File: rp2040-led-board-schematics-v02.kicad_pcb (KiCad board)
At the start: 4 copper layers, 161 x 99 mm, 127 parts, among them J1 PWR_IN, J12 ReceiverRS485, J13 MainBoard, J14 Terminal, J15 Terminal, J16 Terminal, J17 Terminal, J18 Terminal, J19 Terminal, J2 Terminal, J20 Terminal, J5 FrontPanel, J8 ReceiverData, SW1 Button, SW2 PEC16, U1 LM7805, U10 MAX485E, U11 MAX485E, U12 ENC28J60, U13 LM7805, U2 MAX485E, U3 MAX485E, U4 MAX485E, U5 MAX485E, U6 MAX485E, U7 Pico, U8 MAX485E, U9 MAX485E

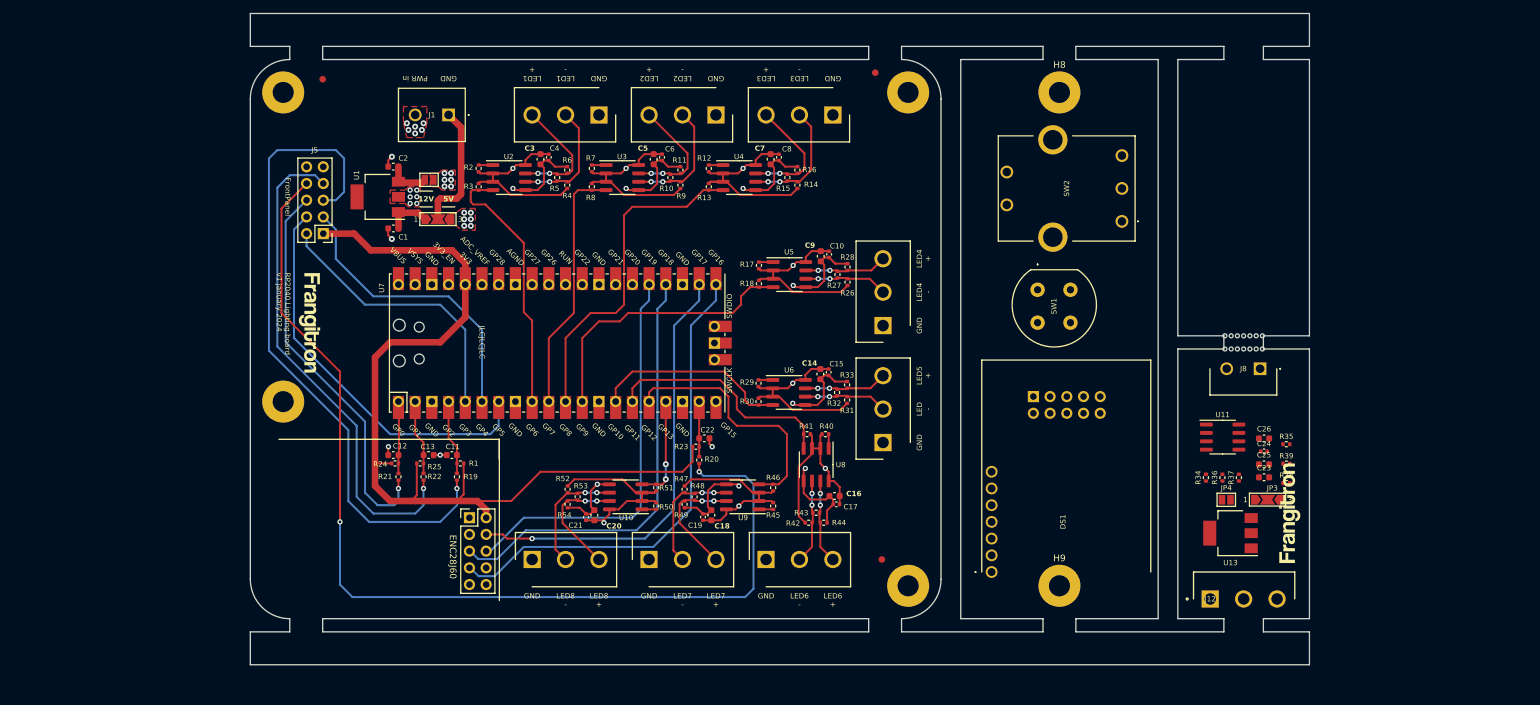
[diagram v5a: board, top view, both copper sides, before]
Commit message: receiver layout OK, some references fixed
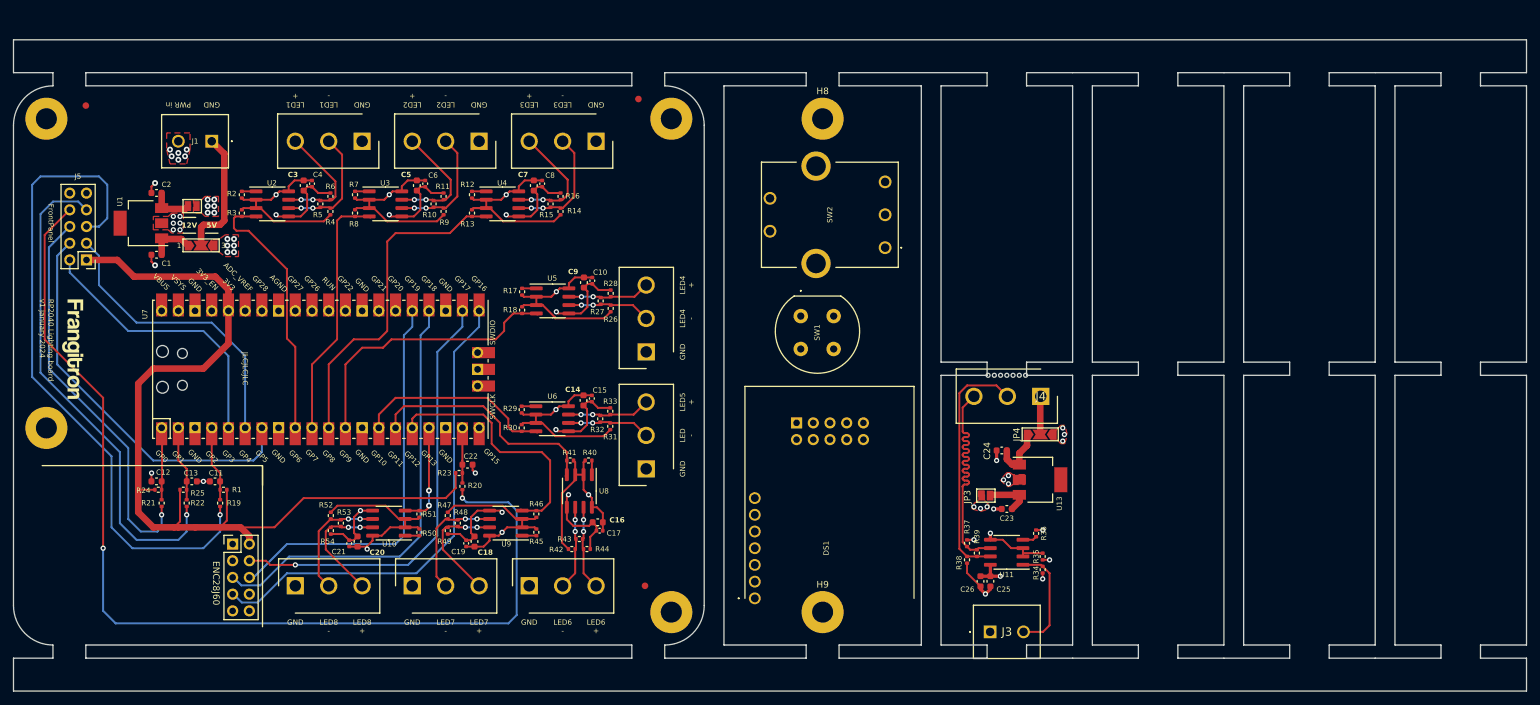
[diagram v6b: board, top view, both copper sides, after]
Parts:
- removed H10: ~, Library:mouse-bites-1x07-jlc
- removed J12: ReceiverRS485, Frangitron:ScrewTerminal_01x03_5.08_Amphenol
- removed J8: ReceiverData, Frangitron:ScrewTerminal_01x02_5.08_Amphenol
- added J3: ReceiverData, Frangitron:ScrewTerminal_01x02_5.08_Amphenol, F.Cu at (186.5, 138.0)
- added J4: ReceiverRS485, Frangitron:ScrewTerminal_01x03_5.08_Amphenol, F.Cu at (194.2, 102.2)
- C24: value 10uF -> 220nF; footprint Capacitor_SMD:C_0402_1005Metric -> Capacitor_SMD:C_0603_1608Metric
- C25: value 220nF -> 100nF
- C26: value 100nF -> 10uF
- H6: moved to B.Cu
- JP3: footprint Jumper:SolderJumper-3_P2.0mm_Open_TrianglePad1.0x1.5mm_NumberLabels -> Jumper:SolderJumper-2_P1.3mm_Open_Pad1.0x1.5mm
- JP4: footprint Jumper:SolderJumper-2_P1.3mm_Open_Pad1.0x1.5mm -> Jumper:SolderJumper-3_P2.0mm_Open_TrianglePad1.0x1.5mm_NumberLabels
- R35: value 20K -> 10K
- R37: value 10K -> 20K
- R38: value 120 -> 20K
- R39: value 20K -> 120
- moved H6 63.0 mm to (173.0, 98.0), turned to -90 degrees
- moved R38 49.9 mm to (182.9, 127.1), turned to -90 degrees
- moved R39 49.0 mm to (184.4, 126.0), turned to 90 degrees
- moved C26 48.3 mm to (185.0, 130.3), turned to -90 degrees
- moved C25 45.2 mm to (186.5, 130.3), turned to -90 degrees
- moved JP3 42.8 mm to (185.8, 117.3)
- moved R37 42.5 mm to (182.9, 124.5), turned to -90 degrees
- moved R35 40.8 mm to (194.4, 126.6), turned to 90 degrees
- moved C24 39.9 mm to (188.2, 110.4), turned to 180 degrees
- moved C23 39.4 mm to (189.0, 119.3), turned to 180 degrees
- moved U11 37.2 mm to (189.0, 125.9), turned to 180 degrees
- moved C5 36.2 mm to (99.3, 70.2)
- moved C7 36.2 mm to (117.1, 70.2)
- moved C9 36.2 mm to (124.7, 84.9)
- moved R12 36.2 mm to (107.7, 71.5)
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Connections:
- net /LED to RS485/D+ renamed /LED to RS485 1/D+
- net /LED to RS485/D- renamed /LED to RS485 1/D-
- net /LED to RS486/D+ renamed /LED to RS485 2/D+
- net /LED to RS486/D- renamed /LED to RS485 2/D-
- net /LED to RS487/D+ renamed /LED to RS485 3/D+
- net /LED to RS487/D- renamed /LED to RS485 3/D-
- net /LED to RS488/D+ renamed /LED to RS485 4/D+
- net /LED to RS488/D- renamed /LED to RS485 4/D-
- net /LED to RS489/D+ renamed /LED to RS485 5/D+
- net /LED to RS489/D- renamed /LED to RS485 5/D-
- net /LED to RS490/D+ renamed /LED to RS485 6/D+
- net /LED to RS490/D- renamed /LED to RS485 6/D-
- net /LED to RS491/D+ renamed /LED to RS485 7/D+
- net /LED to RS491/D- renamed /LED to RS485 7/D-
- net /LED to RS492/D+ renamed /LED to RS485 8/D+
- net /LED to RS492/D- renamed /LED to RS485 8/D-
- net Net-(J12-Pin_2) renamed /Receiver1/D+
- net Net-(J8-Pin_2) renamed /Receiver1/DATA
- C23 pad 2: Recv GND -> /Receiver1/GND
- C24 pad 1: Recv +5V -> /Receiver1/12V
- C24 pad 2: Recv GND -> /Receiver1/GND
- C25 pad 1: Net-(JP4-A) -> /Receiver1/5V
- C25 pad 2: Recv GND -> /Receiver1/GND
- C26 pad 1: Recv +5V -> /Receiver1/5V
- C26 pad 2: Recv GND -> /Receiver1/GND
- JP3 pad 1: Recv +5V -> /Receiver1/5V
- JP4 pad 1: Net-(JP4-A) -> /Receiver1/12V
- JP4 pad 2: Recv PWR -> /Receiver1/PWR IN
- R34 pad 1: Recv +5V -> /Receiver1/5V
- R35 pad 1: Recv +5V -> /Receiver1/5V
- R35 pad 2: Net-(J12-Pin_3) -> /Receiver1/GND
- R36 pad 1: Recv +5V -> /Receiver1/5V
- R36 pad 2: Recv GND -> Net-(U11-DI)
- R37 pad 1: Recv +5V -> /Receiver1/5V
- R37 pad 2: Net-(U11-DI) -> /Receiver1/D-
- R38 pad 2: Net-(J12-Pin_3) -> /Receiver1/GND
- R39 pad 2: Recv GND -> /Receiver1/D-
- U11 pad 2: Recv GND -> /Receiver1/GND
- U11 pad 3: Recv GND -> /Receiver1/GND
- U11 pad 5: Recv GND -> /Receiver1/GND
- U11 pad 6: Net-(J12-Pin_3) -> /Receiver1/D-
- U11 pad 8: Recv +5V -> /Receiver1/5V
- U13 pad 1: Net-(JP4-A) -> /Receiver1/12V
- U13 pad 2: Recv GND -> /Receiver1/GND
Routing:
- net /Receiver1/D+: track 0.00 -> 37.3 mm
- net /Receiver1/D-: track 0.00 -> 37.3 mm
- net /Receiver1/GND: track 0.00 -> 20.9 mm, vias 0 -> 7
- net /Receiver1/DATA: track 0.00 -> 16.9 mm
- net /Receiver1/5V: track 0.00 -> 9.01 mm, vias 0 -> 11
- net /Receiver1/12V: track 0.00 -> 8.63 mm
- net Net-(JP3-B): track 0.00 -> 7.10 mm
- net /Receiver1/PWR IN: track 0.00 -> 5.83 mm
- net Net-(U11-DI): track 0.00 -> 2.19 mm
- added copper zone on F.Cu, net /Receiver1/5V
- added copper zone on In2.Cu, net /Receiver1/5V
- added copper zone on F.Cu, net /Receiver1/GND
- added copper zone on In1.Cu, net /Receiver1/GND
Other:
- board size 161 x 99 mm -> 230 x 99 mm

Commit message: OK for first fabrication review
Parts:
- added C27: 100nF, Capacitor_SMD:C_0603_1608Metric, F.Cu at (190.3, 76.7)
- added C28: 100nF, Capacitor_SMD:C_0603_1608Metric, F.Cu at (191.5, 65.7)
- added C29: 220nF, Capacitor_SMD:C_0603_1608Metric, F.Cu at (191.6, 85.6)
- added C30: 10uF, Capacitor_SMD:C_0402_1005Metric, F.Cu at (193.0, 65.7)
- added C31: 100nF, Capacitor_SMD:C_0603_1608Metric, F.Cu at (210.7, 119.3)
- added C32: 100nF, Capacitor_SMD:C_0603_1608Metric, F.Cu at (209.5, 130.3)
- added C33: 220nF, Capacitor_SMD:C_0603_1608Metric, F.Cu at (209.4, 110.4)
- added C34: 10uF, Capacitor_SMD:C_0402_1005Metric, F.Cu at (208.0, 130.3)
- added C35: 100nF, Capacitor_SMD:C_0603_1608Metric, F.Cu at (213.3, 76.7)
- added C36: 100nF, Capacitor_SMD:C_0603_1608Metric, F.Cu at (214.5, 65.7)
- added C37: 220nF, Capacitor_SMD:C_0603_1608Metric, F.Cu at (214.6, 85.6)
- added C38: 10uF, Capacitor_SMD:C_0402_1005Metric, F.Cu at (216.0, 65.7)
- added C39: 100nF, Capacitor_SMD:C_0603_1608Metric, F.Cu at (233.7, 119.3)
- added C40: 100nF, Capacitor_SMD:C_0603_1608Metric, F.Cu at (232.5, 130.3)
- added C41: 220nF, Capacitor_SMD:C_0603_1608Metric, F.Cu at (232.4, 110.4)
- added C42: 10uF, Capacitor_SMD:C_0402_1005Metric, F.Cu at (231.0, 130.3)
- added C43: 100nF, Capacitor_SMD:C_0603_1608Metric, F.Cu at (236.3, 76.7)
- added C44: 100nF, Capacitor_SMD:C_0603_1608Metric, F.Cu at (237.5, 65.7)
- added C45: 220nF, Capacitor_SMD:C_0603_1608Metric, F.Cu at (237.6, 85.6)
- added C46: 10uF, Capacitor_SMD:C_0402_1005Metric, F.Cu at (239.0, 65.7)
- added C47: 100nF, Capacitor_SMD:C_0603_1608Metric, F.Cu at (256.7, 119.3)
- added C48: 100nF, Capacitor_SMD:C_0603_1608Metric, F.Cu at (255.5, 130.3)
- added C49: 220nF, Capacitor_SMD:C_0603_1608Metric, F.Cu at (255.4, 110.4)
- added C50: 10uF, Capacitor_SMD:C_0402_1005Metric, F.Cu at (254.0, 130.3)
- added C51: 100nF, Capacitor_SMD:C_0603_1608Metric, F.Cu at (259.3, 76.7)
- added C52: 100nF, Capacitor_SMD:C_0603_1608Metric, F.Cu at (260.5, 65.7)
- added C53: 220nF, Capacitor_SMD:C_0603_1608Metric, F.Cu at (260.6, 85.6)
- added C54: 10uF, Capacitor_SMD:C_0402_1005Metric, F.Cu at (262.0, 65.7)
- added FM4: Fiducial, Fiducial:Fiducial_1mm_Mask2mm, F.Cu at (44.5, 145.5)
- added H10: ~, Frangitron:frangitron_logo_16mm, B.Cu at (189.0, 62.0)
- added H12: ~, Library:mouse-bites-1x07-jlc, F.Cu at (189.0, 97.0)
- added H13: ~, Frangitron:frangitron_logo_16mm, B.Cu at (212.0, 134.0)
- added H14: ~, Library:mouse-bites-1x07-jlc, F.Cu at (212.0, 99.0)
- added H15: ~, Frangitron:frangitron_logo_16mm, B.Cu at (212.0, 62.0)
- added H16: ~, Library:mouse-bites-1x07-jlc, F.Cu at (212.0, 97.0)
- added H17: ~, Frangitron:frangitron_logo_16mm, B.Cu at (235.0, 134.0)
- added H18: ~, Library:mouse-bites-1x07-jlc, F.Cu at (235.0, 99.0)
- added H19: ~, Frangitron:frangitron_logo_16mm, B.Cu at (235.0, 62.0)
- added H20: ~, Library:mouse-bites-1x07-jlc, F.Cu at (235.0, 97.0)
- added H21: ~, Frangitron:frangitron_logo_16mm, B.Cu at (258.0, 134.0)
- added H22: ~, Library:mouse-bites-1x07-jlc, F.Cu at (258.0, 99.0)
- added H23: ~, Frangitron:frangitron_logo_16mm, B.Cu at (258.0, 62.0)
- added H24: ~, Library:mouse-bites-1x07-jlc, F.Cu at (258.0, 97.0)
- added H25: MountingHole, MountingHole:MountingHole_2mm, F.Cu at (40.5, 50.5)
- added H26: MountingHole, MountingHole:MountingHole_2mm, F.Cu at (40.5, 144.5)
- added H27: MountingHole, MountingHole:MountingHole_2mm, F.Cu at (265.5, 144.5)
- added H28: MountingHole, MountingHole:MountingHole_2mm, F.Cu at (265.5, 50.5)
- added J10: ReceiverData, Frangitron:ScrewTerminal_01x02_5.08_Amphenol, F.Cu at (214.5, 58.0)
- added J11: ReceiverRS485, Frangitron:ScrewTerminal_01x03_5.08_Amphenol, F.Cu at (206.8, 93.8)
- added J12: ReceiverData, Frangitron:ScrewTerminal_01x02_5.08_Amphenol, F.Cu at (232.5, 138.0)
- added J21: ReceiverRS485, Frangitron:ScrewTerminal_01x03_5.08_Amphenol, F.Cu at (240.2, 102.2)
- added J22: ReceiverData, Frangitron:ScrewTerminal_01x02_5.08_Amphenol, F.Cu at (237.5, 58.0)
- added J23: ReceiverRS485, Frangitron:ScrewTerminal_01x03_5.08_Amphenol, F.Cu at (229.8, 93.8)
- added J24: ReceiverData, Frangitron:ScrewTerminal_01x02_5.08_Amphenol, F.Cu at (255.5, 138.0)
- added J25: ReceiverRS485, Frangitron:ScrewTerminal_01x03_5.08_Amphenol, F.Cu at (263.2, 102.2)
- added J26: ReceiverData, Frangitron:ScrewTerminal_01x02_5.08_Amphenol, F.Cu at (260.5, 58.0)
- added J27: ReceiverRS485, Frangitron:ScrewTerminal_01x03_5.08_Amphenol, F.Cu at (252.8, 93.8)
- added J6: ReceiverData, Frangitron:ScrewTerminal_01x02_5.08_Amphenol, F.Cu at (191.6, 58.0)
- added J7: ReceiverRS485, Frangitron:ScrewTerminal_01x03_5.08_Amphenol, F.Cu at (183.9, 93.8)
- added J8: ReceiverData, Frangitron:ScrewTerminal_01x02_5.08_Amphenol, F.Cu at (209.5, 138.0)
- added J9: ReceiverRS485, Frangitron:ScrewTerminal_01x03_5.08_Amphenol, F.Cu at (217.2, 102.2)
- added JP10: 1-2 12V, Jumper:SolderJumper-3_P2.0mm_Open_TrianglePad1.0x1.5mm_NumberLabels, F.Cu at (206.9, 88.0)
- added JP11: 12V, Jumper:SolderJumper-2_P1.3mm_Open_Pad1.0x1.5mm, F.Cu at (230.5, 117.3)
- added JP12: 1-2 12V, Jumper:SolderJumper-3_P2.0mm_Open_TrianglePad1.0x1.5mm_NumberLabels, F.Cu at (240.1, 108.0)
- added JP13: 12V, Jumper:SolderJumper-2_P1.3mm_Open_Pad1.0x1.5mm, F.Cu at (239.5, 78.7)
- added JP14: 1-2 12V, Jumper:SolderJumper-3_P2.0mm_Open_TrianglePad1.0x1.5mm_NumberLabels, F.Cu at (229.9, 88.0)
- added JP15: 12V, Jumper:SolderJumper-2_P1.3mm_Open_Pad1.0x1.5mm, F.Cu at (253.5, 117.3)
- added JP16: 1-2 12V, Jumper:SolderJumper-3_P2.0mm_Open_TrianglePad1.0x1.5mm_NumberLabels, F.Cu at (263.1, 108.0)
- added JP17: 12V, Jumper:SolderJumper-2_P1.3mm_Open_Pad1.0x1.5mm, F.Cu at (262.5, 78.7)
- added JP18: 1-2 12V, Jumper:SolderJumper-3_P2.0mm_Open_TrianglePad1.0x1.5mm_NumberLabels, F.Cu at (252.9, 88.0)
- added JP5: 12V, Jumper:SolderJumper-2_P1.3mm_Open_Pad1.0x1.5mm, F.Cu at (193.5, 78.7)
- added JP6: 1-2 12V, Jumper:SolderJumper-3_P2.0mm_Open_TrianglePad1.0x1.5mm_NumberLabels, F.Cu at (183.9, 88.0)
- added JP7: 12V, Jumper:SolderJumper-2_P1.3mm_Open_Pad1.0x1.5mm, F.Cu at (207.5, 117.3)
- added JP8: 1-2 12V, Jumper:SolderJumper-3_P2.0mm_Open_TrianglePad1.0x1.5mm_NumberLabels, F.Cu at (217.1, 108.0)
- added JP9: 12V, Jumper:SolderJumper-2_P1.3mm_Open_Pad1.0x1.5mm, F.Cu at (216.5, 78.7)
- added R55: 10K, Resistor_SMD:R_0402_1005Metric, F.Cu at (183.6, 67.4)
- added R56: 10K, Resistor_SMD:R_0402_1005Metric, F.Cu at (183.6, 69.4)
- added R57: 10K, Resistor_SMD:R_0402_1005Metric, F.Cu at (184.6, 73.0)
- added R58: 20K, Resistor_SMD:R_0402_1005Metric, F.Cu at (195.1, 71.1)
- added R59: 20K, Resistor_SMD:R_0402_1005Metric, F.Cu at (195.1, 68.9)
- added R60: 120, Resistor_SMD:R_0402_1005Metric, F.Cu at (193.6, 70.0)
- added R61: 10K, Resistor_SMD:R_0402_1005Metric, F.Cu at (217.4, 128.6)
- added R62: 10K, Resistor_SMD:R_0402_1005Metric, F.Cu at (217.4, 126.6)
- added R63: 10K, Resistor_SMD:R_0402_1005Metric, F.Cu at (216.4, 123.0)
- added R64: 20K, Resistor_SMD:R_0402_1005Metric, F.Cu at (205.9, 124.9)
- added R65: 20K, Resistor_SMD:R_0402_1005Metric, F.Cu at (205.9, 127.1)
- added R66: 120, Resistor_SMD:R_0402_1005Metric, F.Cu at (207.4, 126.0)
- added R67: 10K, Resistor_SMD:R_0402_1005Metric, F.Cu at (206.5, 67.5)
- added R68: 10K, Resistor_SMD:R_0402_1005Metric, F.Cu at (206.5, 69.5)
- added R69: 10K, Resistor_SMD:R_0402_1005Metric, F.Cu at (207.5, 73.0)
- added R70: 20K, Resistor_SMD:R_0402_1005Metric, F.Cu at (218.0, 71.1)
- added R71: 20K, Resistor_SMD:R_0402_1005Metric, F.Cu at (218.0, 69.0)
- added R72: 120, Resistor_SMD:R_0402_1005Metric, F.Cu at (216.5, 70.0)
- added R73: 10K, Resistor_SMD:R_0402_1005Metric, F.Cu at (240.4, 128.6)
- added R74: 10K, Resistor_SMD:R_0402_1005Metric, F.Cu at (240.4, 126.6)
- added R75: 10K, Resistor_SMD:R_0402_1005Metric, F.Cu at (239.4, 123.0)
- added R76: 20K, Resistor_SMD:R_0402_1005Metric, F.Cu at (228.9, 124.9)
- added R77: 20K, Resistor_SMD:R_0402_1005Metric, F.Cu at (228.9, 127.1)
- added R78: 120, Resistor_SMD:R_0402_1005Metric, F.Cu at (230.4, 126.0)
- added R79: 10K, Resistor_SMD:R_0402_1005Metric, F.Cu at (229.5, 67.5)
- added R80: 10K, Resistor_SMD:R_0402_1005Metric, F.Cu at (229.5, 69.5)
- added R81: 10K, Resistor_SMD:R_0402_1005Metric, F.Cu at (230.5, 73.0)
- added R82: 20K, Resistor_SMD:R_0402_1005Metric, F.Cu at (241.0, 71.1)
- added R83: 20K, Resistor_SMD:R_0402_1005Metric, F.Cu at (241.0, 69.0)
- added R84: 120, Resistor_SMD:R_0402_1005Metric, F.Cu at (239.5, 70.0)
- added R85: 10K, Resistor_SMD:R_0402_1005Metric, F.Cu at (263.4, 128.6)
- added R86: 10K, Resistor_SMD:R_0402_1005Metric, F.Cu at (263.4, 126.6)
- added R87: 10K, Resistor_SMD:R_0402_1005Metric, F.Cu at (262.4, 123.0)
- added R88: 20K, Resistor_SMD:R_0402_1005Metric, F.Cu at (251.9, 124.9)
- added R89: 20K, Resistor_SMD:R_0402_1005Metric, F.Cu at (251.9, 127.1)
- added R90: 120, Resistor_SMD:R_0402_1005Metric, F.Cu at (253.4, 126.0)
- added R91: 10K, Resistor_SMD:R_0402_1005Metric, F.Cu at (252.6, 67.5)
- added R92: 10K, Resistor_SMD:R_0402_1005Metric, F.Cu at (252.6, 69.5)
- added R93: 10K, Resistor_SMD:R_0402_1005Metric, F.Cu at (253.5, 73.0)
- added R94: 20K, Resistor_SMD:R_0402_1005Metric, F.Cu at (264.0, 71.1)
- added R95: 20K, Resistor_SMD:R_0402_1005Metric, F.Cu at (264.0, 69.0)
- added R96: 120, Resistor_SMD:R_0402_1005Metric, F.Cu at (262.5, 70.0)
- added U14: MAX485E, Package_SO:SOIC-8_3.9x4.9mm_P1.27mm, F.Cu at (189.0, 70.1)
- added U15: LM7805, Package_TO_SOT_SMD:SOT-223, F.Cu at (185.8, 81.1)
- added U16: MAX485E, Package_SO:SOIC-8_3.9x4.9mm_P1.27mm, F.Cu at (212.0, 125.9)
- added U17: LM7805, Package_TO_SOT_SMD:SOT-223, F.Cu at (215.2, 114.9)
- added U18: MAX485E, Package_SO:SOIC-8_3.9x4.9mm_P1.27mm, F.Cu at (212.0, 70.1)
- added U19: LM7805, Package_TO_SOT_SMD:SOT-223, F.Cu at (208.8, 81.1)
- added U20: MAX485E, Package_SO:SOIC-8_3.9x4.9mm_P1.27mm, F.Cu at (235.0, 125.9)
- added U21: LM7805, Package_TO_SOT_SMD:SOT-223, F.Cu at (238.2, 114.9)
- added U22: MAX485E, Package_SO:SOIC-8_3.9x4.9mm_P1.27mm, F.Cu at (235.0, 70.1)
- added U23: LM7805, Package_TO_SOT_SMD:SOT-223, F.Cu at (231.8, 81.1)
- added U24: MAX485E, Package_SO:SOIC-8_3.9x4.9mm_P1.27mm, F.Cu at (258.0, 125.9)
- added U25: LM7805, Package_TO_SOT_SMD:SOT-223, F.Cu at (261.2, 114.9)
- added U26: MAX485E, Package_SO:SOIC-8_3.9x4.9mm_P1.27mm, F.Cu at (258.0, 70.1)
- added U27: LM7805, Package_TO_SOT_SMD:SOT-223, F.Cu at (254.8, 81.1)
- moved FM2 128.7 mm to (261.5, 49.5)
- moved FM3 128.3 mm to (261.5, 145.5)
- moved FM1 9.39 mm to (45.0, 49.5)
- moved U13 1.86 mm to (192.2, 114.9)
- moved C24 1.85 mm to (186.4, 110.4)
- moved C23 1.27 mm to (187.7, 119.3)
- moved JP3 1.27 mm to (184.5, 117.3)
- moved R37 0.38 mm to (182.9, 124.9)
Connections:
- net /Receiver1/12V renamed /Receiver 1/12V
- net /Receiver1/5V renamed /Receiver 1/5V
- net /Receiver1/D+ renamed /Receiver 1/D+
- net /Receiver1/D- renamed /Receiver 1/D-
- net /Receiver1/DATA renamed /Receiver 1/DATA
- net /Receiver1/GND renamed /Receiver 1/GND
- net /Receiver1/PWR IN renamed /Receiver 1/PWR IN
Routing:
- net /Receiver 2/D-: track 0.00 -> 40.3 mm
- net /Receiver 7/D-: track 0.00 -> 40.3 mm
- net /Receiver 3/D-: track 0.00 -> 40.3 mm
- net /Receiver 5/D-: track 0.00 -> 40.3 mm
- net /Receiver 4/D-: track 0.00 -> 40.3 mm
- net /Receiver 6/D-: track 0.00 -> 40.3 mm
- net /Receiver 8/D-: track 0.00 -> 40.3 mm
- net /Receiver 8/D+: track 0.00 -> 40.3 mm
- net /Receiver 7/D+: track 0.00 -> 40.3 mm
- net /Receiver 6/D+: track 0.00 -> 40.3 mm
- net /Receiver 5/D+: track 0.00 -> 40.3 mm
- net /Receiver 4/D+: track 0.00 -> 40.3 mm
- net /Receiver 3/D+: track 0.00 -> 40.3 mm
- net /Receiver 2/D+: track 0.00 -> 40.3 mm
- net /Receiver 7/GND: track 0.00 -> 20.9 mm, vias 0 -> 7
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- added copper zone on F.Cu, net /Receiver 2/5V
- added copper zone on In2.Cu, net /Receiver 2/5V
- added copper zone on F.Cu, net /Receiver 2/GND
- added copper zone on In1.Cu, net /Receiver 2/GND
- added copper zone on F.Cu, net /Receiver 3/5V
- added copper zone on In2.Cu, net /Receiver 3/5V
- added copper zone on F.Cu, net /Receiver 3/GND
- added copper zone on In1.Cu, net /Receiver 3/GND
- added copper zone on F.Cu, net /Receiver 4/5V
- added copper zone on In2.Cu, net /Receiver 4/5V
- added copper zone on F.Cu, net /Receiver 4/GND
- added copper zone on In1.Cu, net /Receiver 4/GND
- added copper zone on F.Cu, net /Receiver 5/5V
- added copper zone on In2.Cu, net /Receiver 5/5V
- added copper zone on F.Cu, net /Receiver 5/GND
- added copper zone on In1.Cu, net /Receiver 5/GND
- added copper zone on F.Cu, net /Receiver 6/5V
- added copper zone on In2.Cu, net /Receiver 6/5V
- added copper zone on F.Cu, net /Receiver 6/GND
- added copper zone on In1.Cu, net /Receiver 6/GND
- added copper zone on F.Cu, net /Receiver 7/5V
- added copper zone on In2.Cu, net /Receiver 7/5V
- added copper zone on F.Cu, net /Receiver 7/GND
- added copper zone on In1.Cu, net /Receiver 7/GND
- added copper zone on F.Cu, net /Receiver 8/5V
- added copper zone on In2.Cu, net /Receiver 8/5V
- added copper zone on F.Cu, net /Receiver 8/GND
- added copper zone on In1.Cu, net /Receiver 8/GND

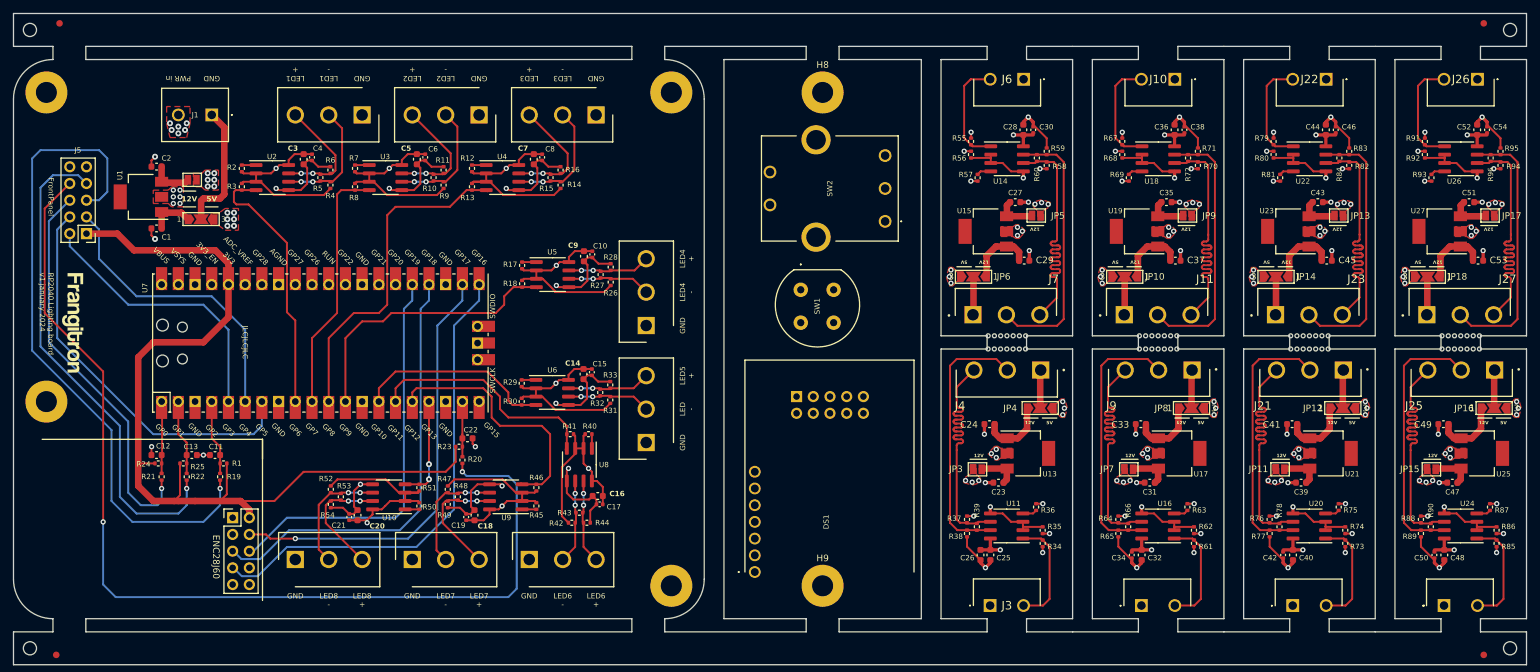
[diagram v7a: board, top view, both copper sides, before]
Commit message: unify receiver layout, reduce global heigt by 1mm for symmetry
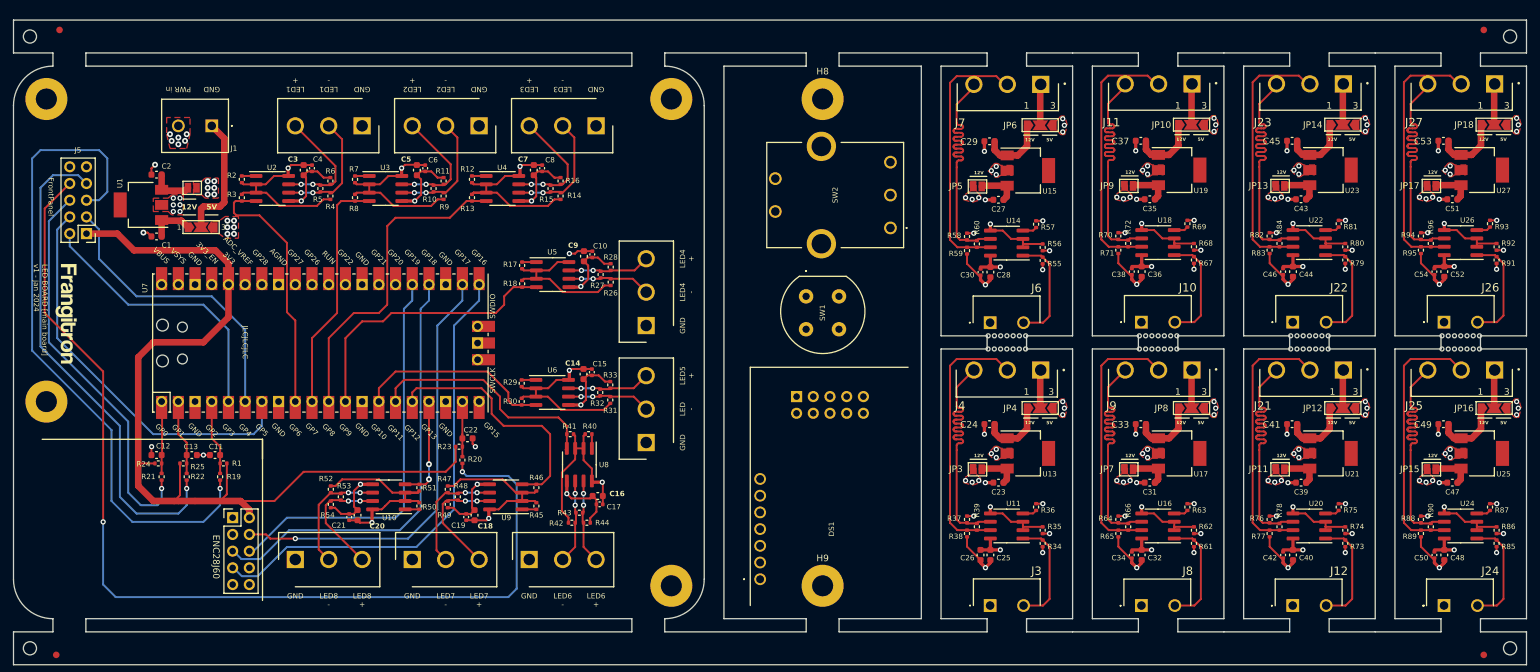
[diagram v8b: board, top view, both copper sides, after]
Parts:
- moved J6 37.4 mm to (186.5, 95.0), turned to 0 degrees
- moved J10 37.3 mm to (209.5, 94.9), turned to 0 degrees
- moved J22 37.3 mm to (232.5, 94.9), turned to 0 degrees
- moved J26 37.3 mm to (255.5, 94.9), turned to 0 degrees
- moved J27 36.6 mm to (263.2, 58.7), turned to 180 degrees
- moved J11 36.6 mm to (217.2, 58.7), turned to 180 degrees
- moved J23 36.6 mm to (240.2, 58.7), turned to 180 degrees
- moved J7 36.5 mm to (194.2, 58.8), turned to 180 degrees
- moved H13 28.0 mm to (211.5, 106.0)
- moved H17 28.0 mm to (234.5, 106.0)
- moved H21 28.0 mm to (257.5, 106.0)
- moved H7 28.0 mm to (188.5, 106.0)
- moved JP18 25.2 mm to (263.1, 64.9), turned to 0 degrees
- moved JP10 25.2 mm to (217.1, 64.9), turned to 0 degrees
- moved JP14 25.2 mm to (240.1, 64.9), turned to 0 degrees
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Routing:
- net GND: track 111.0 -> 96.3 mm
- net LED3 out: track 51.1 -> 49.5 mm
- net LED2 out: track 38.5 -> 36.8 mm
- net +5V: track 232.7 -> 234.2 mm
- net LED7 out: track 38.8 -> 38.0 mm
- net LED1 out: track 40.6 -> 39.9 mm
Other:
- board size 230 x 99 mm -> 230 x 98 mm
- board text added: "LED BOARD [front panel] v1 - jan 2024"
- board text added: "LED BOARD [main board] v1 - jan 2024"
- board text added: "LED BOARD [receiver] v1 - jan 2024"
- board text added: "locked"
- board text removed: "<-- V-CUT"
- board text removed: "RP2040 Lighting board v1 january 2024"
- board text removed: "V-CUT -->"
